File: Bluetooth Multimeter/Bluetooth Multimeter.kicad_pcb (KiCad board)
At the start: 2 copper layers, 55 x 90 mm, 33 parts, among them J1 V/Ohm, J2 Com, J3 mA, J4 A, J5 Parallel Prot, J6 3.3V, J7 GND, K1 Low Range, K2 Medium Range, K3 High Range, K4 UH Range (Ohm Only), K5 V/Ohm Switch, U1 ItsyBitsy_NRF52840_Big

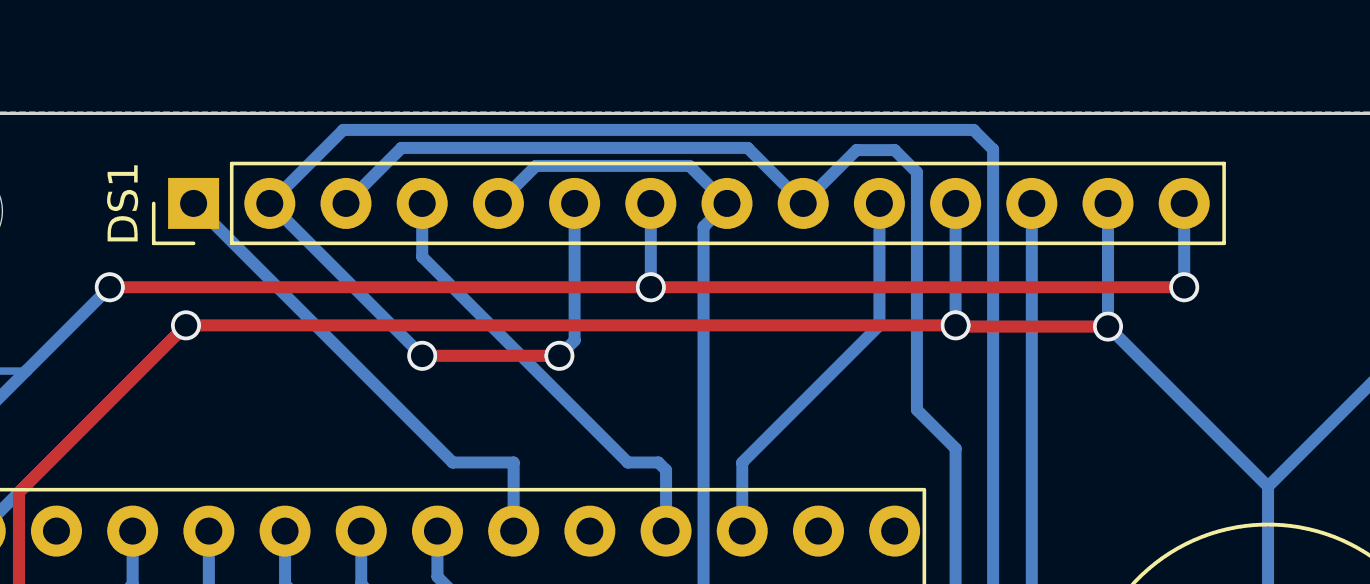
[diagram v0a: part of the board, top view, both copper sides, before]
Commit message: fixed itsybitsy footprint and lcd connection
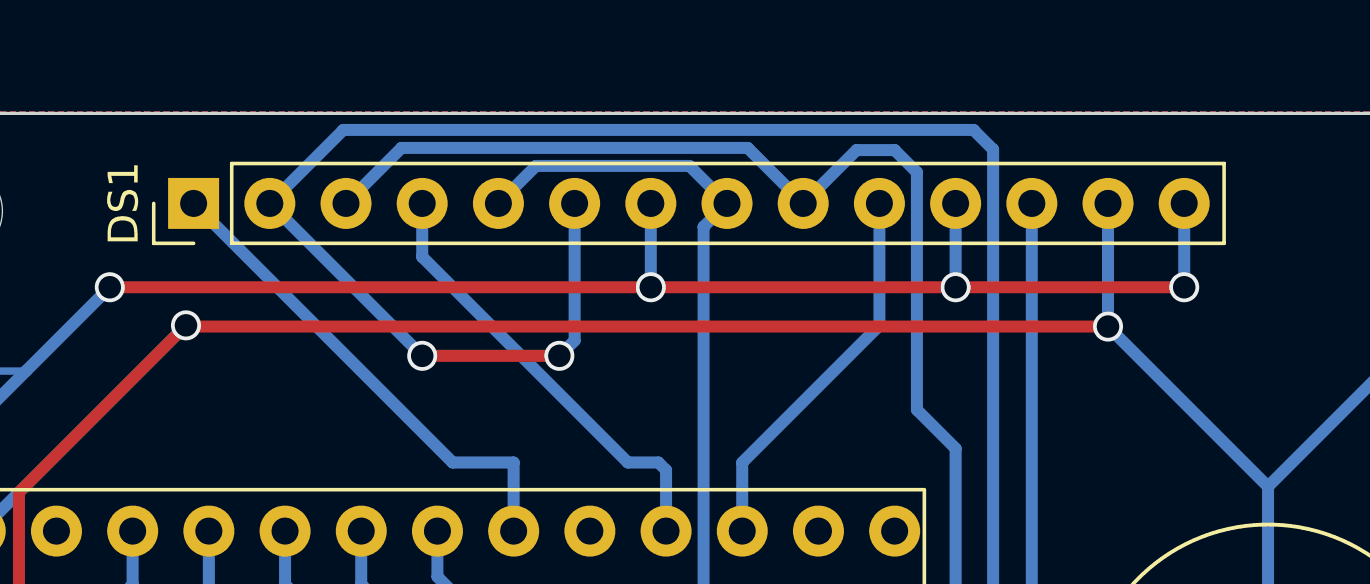
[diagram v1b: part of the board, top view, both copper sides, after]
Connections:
- DS1 pad 11: GND -> +3.3V
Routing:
- net GND: track 190.1 -> 186.1 mm, vias 3 -> 2
- net +3.3V: track 70.6 -> 73.4 mm, vias 3 -> 4
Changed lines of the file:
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@@
       (drillshape 0)
       (scaleselection 1)
-      (outputdirectory "Bluetooth Multimeter rev4 toshop/")
+      (outputdirectory "Bluetooth Multimeter toshop/")
     )
   )
@@
       (net 21 "/TFT DC") (pinfunction "DC") (pintype "passive"))
     (pad "11" thru_hole oval (at 0 25.4 90) (size 1.7 1.7) (drill 0.9) (layers "*.Cu" "*.Mask")
-      (net 2 "GND") (pinfunction "RESET") (pintype "passive"))
+      (net 1 "+3.3V") (pinfunction "RESET") (pintype "passive"))
     (pad "12" thru_hole oval (at 0 27.94 90) (size 1.7 1.7) (drill 0.9) (layers "*.Cu" "*.Mask")
       (net 22 "/TFT CS") (pinfunction "CS") (pintype "passive"))
@@
   (gr_rect (start 120.318 53.388) (end 175.318 143.388)
     (stroke (width 0.1) (type default)) (fill none) (layer "Edge.Cuts"))
+  (segment (start 156.718 59.182) (end 146.558 59.182) (width 0.4) (layer "F.Cu") (net 1))
   (segment (start 146.558 59.182) (end 128.524 59.182) (width 0.4) (layer "F.Cu") (net 1))
-  (segment (start 164.338 59.182) (end 146.558 59.182) (width 0.4) (layer "F.Cu") (net 1))
+  (segment (start 164.338 59.182) (end 156.718 59.182) (width 0.4) (layer "F.Cu") (net 1))
   (via (at 164.338 59.182) (size 1) (drill 0.75) (layers "F.Cu" "B.Cu") (net 1))
   (via (at 146.558 59.182) (size 1) (drill 0.75) (layers "F.Cu" "B.Cu") (net 1))
+  (via (at 156.718 59.182) (size 1) (drill 0.75) (layers "F.Cu" "B.Cu") (net 1))
   (via (at 128.524 59.182) (size 1) (drill 0.75) (layers "F.Cu" "B.Cu") (net 1))
   (segment (start 122.682 61.976) (end 125.73 61.976) (width 0.25) (layer "B.Cu") (net 1))
   (segment (start 122.956 81.3) (end 124.206 82.55) (width 0.4) (layer "B.Cu") (net 1))
+  (segment (start 156.718 56.388) (end 156.718 59.182) (width 0.4) (layer "B.Cu") (net 1))
   (segment (start 128.524 59.182) (end 125.73 61.976) (width 0.4) (layer "B.Cu") (net 1))
   (segment (start 122.956 64.75) (end 122.956 81.3) (width 0.4) (layer "B.Cu") (net 1))
@@
   (segment (start 164.338 56.388) (end 164.338 59.182) (width 0.4) (layer "B.Cu") (net 1))
   (segment (start 125.73 61.976) (end 122.956 64.75) (width 0.4) (layer "B.Cu") (net 1))
+  (segment (start 131.104 60.492) (end 161.798 60.492) (width 0.4) (layer "F.Cu") (net 2))
   (segment (start 141.732 92.456) (end 143.764 94.488) (width 0.4) (layer "F.Cu") (net 2))
   (segment (start 128.27 94.488) (end 130.302 92.456) (width 0.4) (layer "F.Cu") (net 2))
   (segment (start 130.302 92.456) (end 141.732 92.456) (width 0.4) (layer "F.Cu") (net 2))
-  (segment (start 131.064 60.452) (end 156.718 60.452) (width 0.4) (layer "F.Cu") (net 2))
   (segment (start 128.016 90.17) (end 128.016 75.946) (width 0.4) (layer "F.Cu") (net 2))
   (segment (start 125.496 66.02) (end 131.064 60.452) (width 0.4) (layer "F.Cu") (net 2))
-  (segment (start 156.758 60.492) (end 156.718 60.452) (width 0.4) (layer "F.Cu") (net 2))
   (segment (start 128.016 75.946) (end 125.496 73.426) (width 0.4) (layer "F.Cu") (net 2))
-  (segment (start 161.798 60.492) (end 156.758 60.492) (width 0.4) (layer "F.Cu") (net 2))
+  (segment (start 131.064 60.452) (end 131.104 60.492) (width 0.4) (layer "F.Cu") (net 2))
   (segment (start 125.496 73.426) (end 125.496 66.02) (width 0.4) (layer "F.Cu") (net 2))
   (segment (start 130.302 92.456) (end 128.016 90.17) (width 0.4) (layer "F.Cu") (net 2))
-  (via (at 156.718 60.452) (size 1) (drill 0.75) (layers "F.Cu" "B.Cu") (net 2))
   (via (at 161.798 60.492) (size 1) (drill 0.75) (layers "F.Cu" "B.Cu") (net 2))
   (via (at 131.064 60.452) (size 1) (drill 0.75) (layers "F.Cu" "B.Cu") (net 2))
@@
   (segment (start 170.982 61.976) (end 172.974 61.976) (width 0.4) (layer "B.Cu") (net 2))
   (segment (start 167.132 65.826) (end 170.982 61.976) (width 0.4) (layer "B.Cu") (net 2))
-  (segment (start 156.718 56.388) (end 156.718 60.452) (width 0.4) (layer "B.Cu") (net 2))
   (segment (start 156.464 106.172) (end 154.432 108.204) (width 0.4) (layer "B.Cu") (net 2))
   (segment (start 143.764 105.664) (end 143.764 104.394) (width 0.4) (layer "B.Cu") (net 2))

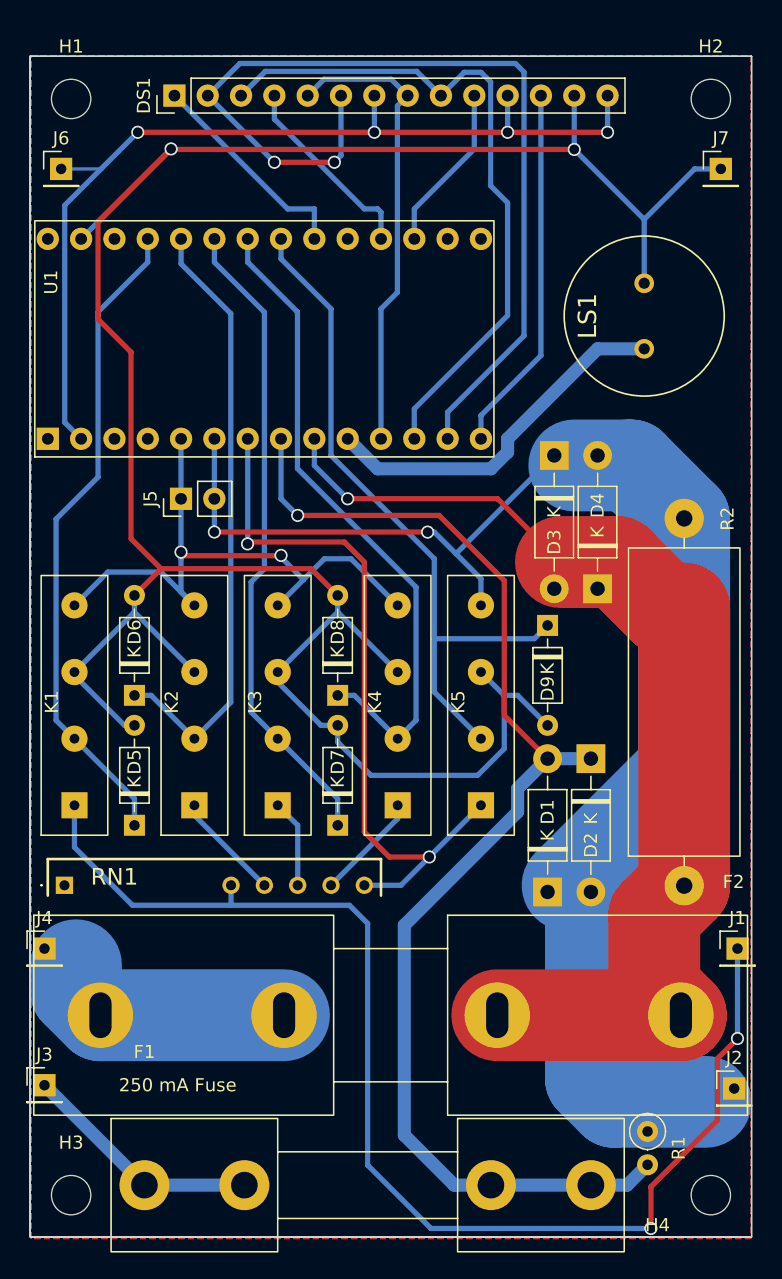
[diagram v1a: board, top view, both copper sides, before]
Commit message: pcb modifications based on first shop board
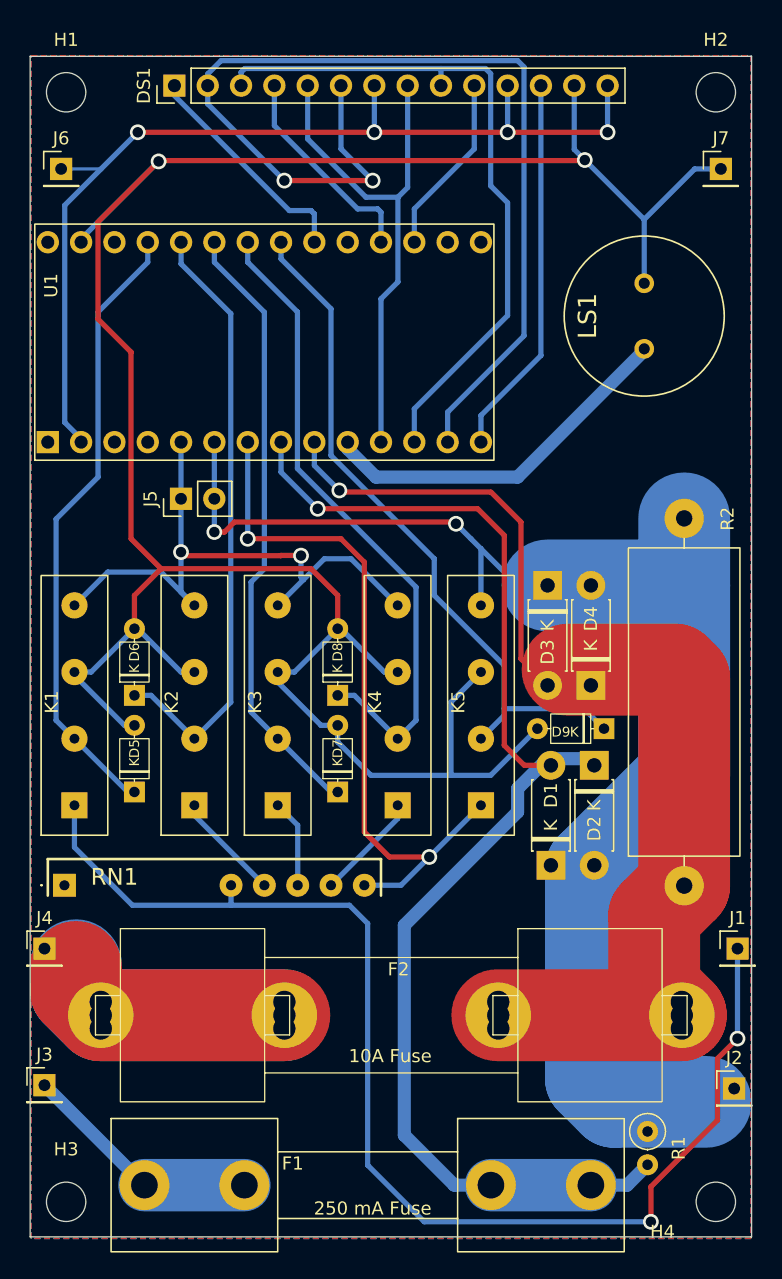
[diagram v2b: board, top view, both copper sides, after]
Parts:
- D1, D2, D3, D4: footprint Diode_THT:D_DO-41_SOD81_P10.16mm_Horizontal -> Diode_THT:D_DO-41_SOD81_P7.62mm_Horizontal
- D5, D6, D7, D8, D9: footprint Diode_THT:D_DO-35_SOD27_P7.62mm_Horizontal -> 502ProjectFootprints:D_DO-35_SOD27_P5.08mm_Horizontal
- DS1: footprint 502ProjectFootprints:PinHeader_1x14_P2.54mm_Vertical_H0.9mm -> 502ProjectFootprints:PinHeader_1x14_P2.54mm_Vertical_H1.0
- F2: footprint 502ProjectFootprints:LF124041_4 -> 502ProjectFootprints:LF124041_6
- J1, J2, J3, J4, J6, J7: footprint 502ProjectFootprints:PinHeader_1x01_P2.54mm_Vertical_H0.8mm -> 502ProjectFootprints:PinHeader_1x01_P2.54mm_Vertical_H0.9mm
- moved F2 10.1 mm to (156.0, 126.5)
- moved D3 9.92 mm to (159.8, 93.7)
- moved D9 8.97 mm to (164.1, 104.6), turned to 180 degrees
- moved D4 7.38 mm to (163.1, 101.3)
- moved D5 2.54 mm to (128.3, 109.5)
- moved D7 2.54 mm to (143.8, 109.5)
- moved D1 2.05 mm to (160.0, 115.1)
- moved DS1 0.76 mm to (131.3, 55.6)
- moved H3 0.64 mm to (123.1, 140.7)
- moved H4 0.64 mm to (172.6, 140.7)
- moved H1 0.64 mm to (123.1, 56.1)
- moved H2 0.64 mm to (172.6, 56.1)
- moved D2 0.57 mm to (163.3, 107.4)
- moved U1 0.25 mm to (138.2, 75.2)
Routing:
- net /A In: track 18.6 -> 37.0 mm
- net /MISO: track 72.8 -> 80.2 mm
- net /Input Common: track 110.3 -> 104.7 mm
- net /SCK: track 35.7 -> 39.0 mm
- net /mA ADC In: track 96.4 -> 99.0 mm
- net /High Range Control: track 49.4 -> 47.2 mm
- net /Low Range Control: track 50.1 -> 47.8 mm
- net /A ADC In: track 81.5 -> 83.5 mm
- net GND: track 186.1 -> 187.0 mm
- net /V/Ohm ADC In: track 47.3 -> 48.2 mm
- net /V/Ohm In: track 95.6 -> 94.9 mm
- net /MOSI: track 52.3 -> 52.9 mm
- net /V/Ohm Control: track 53.5 -> 54.1 mm
- net /Ohm Vout: track 55.3 -> 54.7 mm

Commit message: finalized rev 2 board to be milled
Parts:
- F1: footprint 502ProjectFootprints:LF124061_1 -> 502ProjectFootprints:LF124061_3
- moved F1 10.7 mm to (136.1, 138.4)
- moved J3 2.70 mm to (123.2, 133.9)
- moved J2 2.18 mm to (172.7, 133.9)
- moved J4 1.80 mm to (123.2, 121.2)
- moved J1 1.63 mm to (173.2, 122.7)
- moved F2 1.52 mm to (154.5, 126.5)
- moved D9 0.13 mm to (164.1, 104.8)
- moved D5 0.11 mm to (128.3, 109.6)
- moved D6 0.11 mm to (128.3, 102.2)
- moved D7 0.11 mm to (143.8, 109.6)
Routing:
- net GND: track 187.0 -> 210.6 mm
- net /A ADC In: track 83.5 -> 99.9 mm
- net /UH Range Control: track 49.9 -> 65.7 mm
- net /MISO: track 80.2 -> 70.7 mm
- net /Input Common: track 104.7 -> 113.9 mm
- net /mA ADC In: track 99.0 -> 107.7 mm
- net /mA In: track 18.4 -> 24.4 mm
- net /V/Ohm ADC In: track 48.2 -> 54.0 mm
- net /A In: track 37.0 -> 31.2 mm
- net /V/Ohm In: track 94.9 -> 90.2 mm
- net /V/Ohm Control: track 54.1 -> 57.7 mm
- net /TOUCH CS: track 15.2 -> 17.8 mm
- net /SCK: track 39.0 -> 41.1 mm
- net /Low Range Control: track 47.8 -> 49.6 mm
- net /Med Range Control: track 46.8 -> 48.4 mm
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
